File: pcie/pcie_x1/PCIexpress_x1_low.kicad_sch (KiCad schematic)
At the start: 2 parts, among them J2 PCIexpress_x1, U1 XC7A50T-FGG484

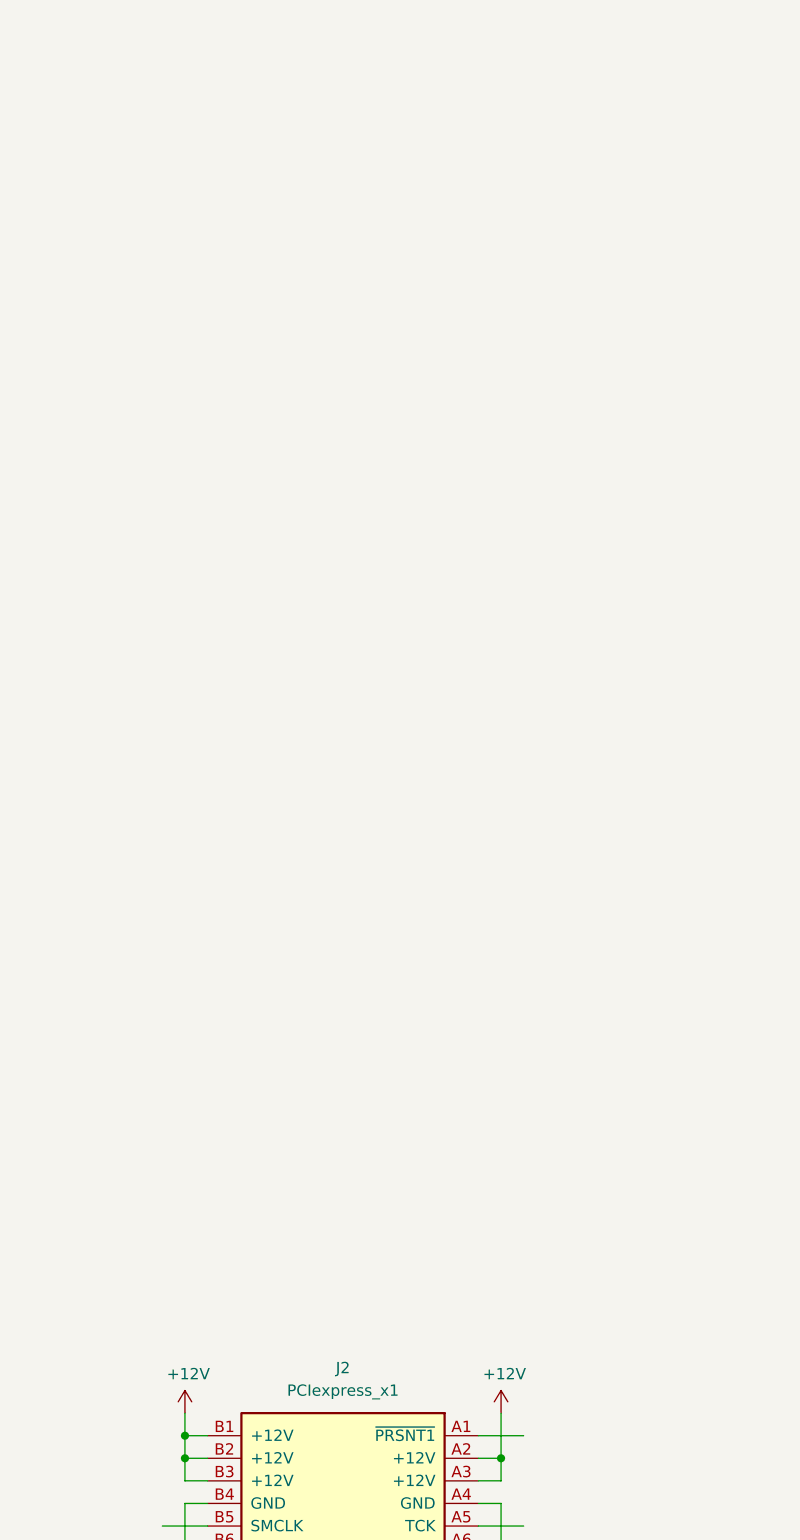
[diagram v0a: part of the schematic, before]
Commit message: working on x1 pcie card
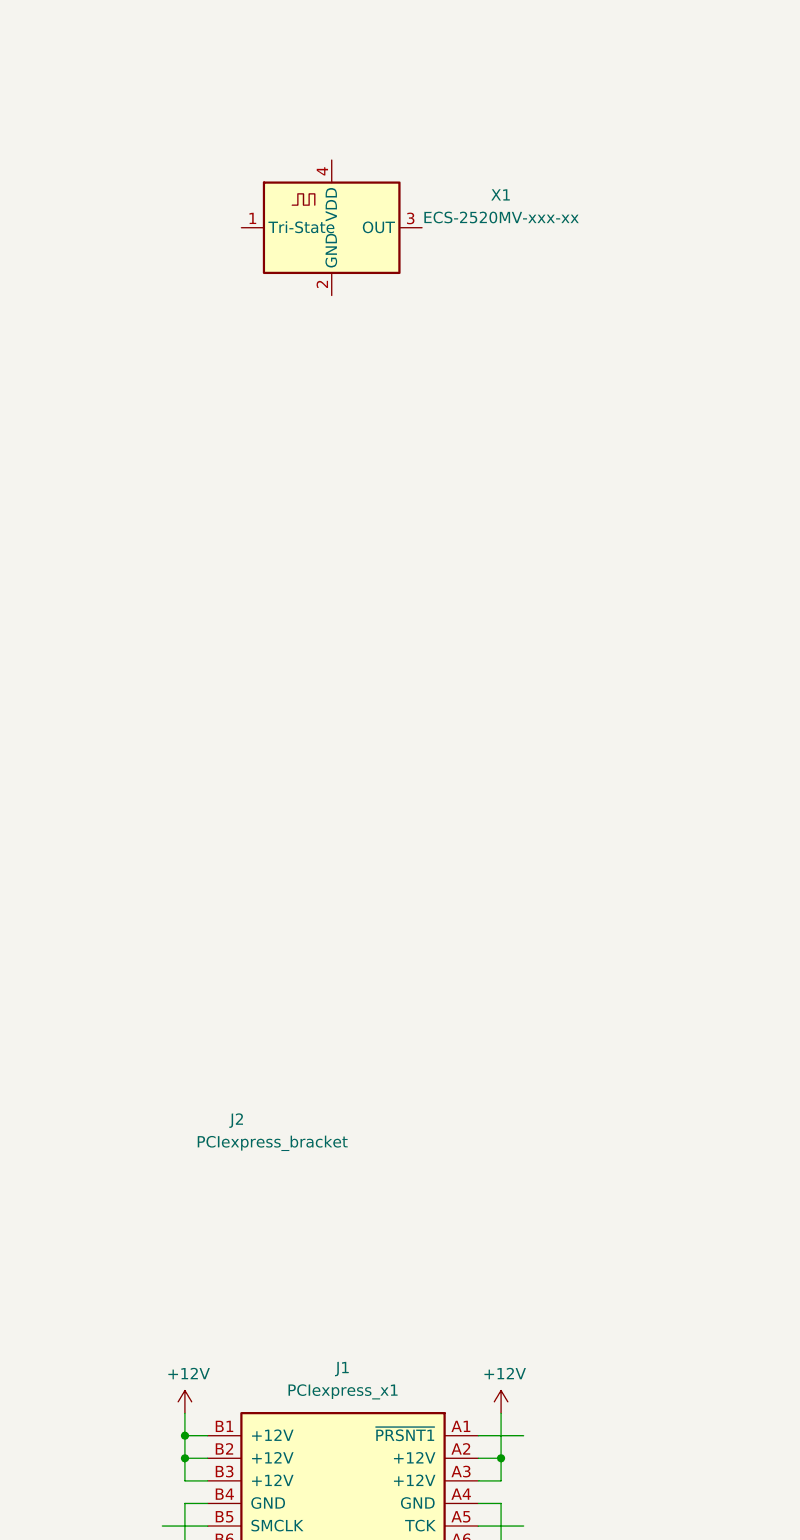
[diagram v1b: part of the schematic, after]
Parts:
- added J2: PCIexpress_bracket, pedrolib:PCIexpress_bracket_low, symbol pedrolib:PCIexpress_bracket
- added X1: ECS-2520MV-xxx-xx, pedrolib:OSC_ECS-2520S25-250-FN-TR, symbol pedrolib:ECS-2520MV-xxx-xx
- renumbered J2 to J1
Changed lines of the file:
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@@
     (effects (font (size 1.27 1.27)) (justify left bottom))
   )
+  (symbol (lib_id "pedrolib:PCIexpress_bracket") (at 59.69 323.85 0) (unit 1)
+    (in_bom yes) (on_board yes) (dnp no)
+    (property "Reference" "J2" (at 64.77 322.58 0)
+      (effects (font (size 1.27 1.27)) (justify left))
+    )
+    (property "Value" "PCIexpress_bracket" (at 60.96 325.12 0)
+      (effects (font (size 1.27 1.27)) (justify left))
+    )
+    (property "Footprint" "pedrolib:PCIexpress_bracket_low" (at 59.69 323.85 0)
+      (effects (font (size 1.27 1.27)) hide)
+    )
+    (property "Datasheet" "" (at 59.69 323.85 0)
+      (effects (font (size 1.27 1.27)) hide)
+    )
+    (instances
+      (project "PCIexpress_x1_low"
+        (path "/b58173cd-28d5-49a4-a789-299fbf6f5cc2"
+          (reference "J2") (unit 1)
+        )
+      )
+    )
+  )
   (symbol (lib_id "FPGA_Xilinx_Artix7:XC7A50T-FGG484") (at 78.74 88.9 0) (unit 1)
     (in_bom yes) (on_board yes) (dnp no) (fields_autoplaced)
@@
   (symbol (lib_id "pedrolib:PCIexpress_x1") (at 77.47 355.6 0) (unit 1)
     (in_bom yes) (on_board yes) (dnp no) (fields_autoplaced)
-    (property "Reference" "J2" (at 77.47 350.52 0)
+    (property "Reference" "J1" (at 77.47 350.52 0)
       (effects (font (size 1.27 1.27)))
     )
@@
       (project "PCIexpress_x1_low"
         (path "/b58173cd-28d5-49a4-a789-299fbf6f5cc2"
-          (reference "J2") (unit 1)
+          (reference "J1") (unit 1)
         )
       )
@@
         )
       )
+    )
+  )
+  (symbol (lib_id "pedrolib:ECS-2520MV-xxx-xx") (at 76.2 222.25 0) (unit 1)
+    (in_bom yes) (on_board yes) (dnp no) (fields_autoplaced)
+    (property "Reference" "X1" (at 95.25 218.6021 0)
+      (effects (font (size 1.27 1.27)))
+    )
+    (property "Value" "ECS-2520MV-xxx-xx" (at 95.25 221.1421 0)
+      (effects (font (size 1.27 1.27)))
+    )
+    (property "Footprint" "pedrolib:OSC_ECS-2520S25-250-FN-TR" (at 87.63 231.14 0)
+      (effects (font (size 1.27 1.27)) hide)
+    )
+    (property "Datasheet" "https://www.ecsxtal.com/store/pdf/ECS-2520MV.pdf" (at 71.755 219.075 0)
+      (effects (font (size 1.27 1.27)) hide)
+    )
+    (pin "1")
+    (pin "2")
+    (pin "3")
+    (pin "4")
+    (instances
+      (project "PCIexpress_x1_low"
+        (path "/b58173cd-28d5-49a4-a789-299fbf6f5cc2"
+          (reference "X1") (unit 1)
+        )
+      )
